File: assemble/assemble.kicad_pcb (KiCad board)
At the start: 2 copper layers, 283.6 x 105.3 mm, 94 parts, among them J1 Conn_01x04, SW1 SW_Push, SW10 SW_Push, SW11 SW_Push, SW12 SW_Push, SW13 SW_Push, SW14 SW_Push, SW15 SW_Push, SW16 SW_Push, SW17 SW_Push, SW18 SW_Push, SW19 SW_Push, SW2 SW_Push, SW20 SW_Push, SW21 SW_Push, SW22 SW_Push, SW23 SW_Push, SW24 SW_Push, SW25 SW_Push, SW26 SW_Push, SW27 SW_Push, SW28 SW_Push, SW29 SW_Push, SW3 SW_Push, SW30 SW_Push, SW31 SW_Push, SW32 SW_Push, SW33 SW_Push, SW34 SW_Push, SW35 SW_Push, SW36 SW_Push, SW37 SW_Push, SW38 SW_Push, SW39 SW_Push, SW4 SW_Push, SW40 SW_Push, SW41 SW_Push, SW42 SW_Push, SW45 RotaryEncoder_Switch, SW46 RotaryEncoder_Switch, SW47 SW_SPDT, SW5 SW_Push, SW6 SW_Push, SW7 SW_Push, SW8 SW_Push, SW9 SW_Push, U1 XIAO-nRF52840-SMD, U4 XIAO-nRF52840-SMD

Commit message: feat: implement schematic and PCB partially
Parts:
- removed U4: XIAO-nRF52840-SMD, xiao:XIAO-nRF52840-SMD
- added D43: D, kbd_Parts:Diode_SMD, F.Cu at (245.8, 104.6)
- added D44: D, kbd_Parts:Diode_SMD, F.Cu at (251.7, 104.6)
- added D45: D, kbd_Parts:Diode_SMD, F.Cu at (257.7, 104.6)
- added D46: D, kbd_Parts:Diode_SMD, F.Cu at (263.4, 112.6)
- added D47: D, kbd_Parts:Diode_SMD, F.Cu at (245.8, 112.6)
- added D48: D, kbd_Parts:Diode_SMD, F.Cu at (218.6, 52.2)
- added D49: D, kbd_Parts:Diode_SMD, F.Cu at (222.6, 69.4)
- added D50: D, kbd_Parts:Diode_SMD, F.Cu at (225.6, 85.8)
- added D51: D, kbd_Parts:Diode_SMD, F.Cu at (251.7, 112.6)
- added D52: D, kbd_Parts:Diode_SMD, F.Cu at (235.8, 52.6)
- added D53: D, kbd_Parts:Diode_SMD, F.Cu at (238.6, 69.4)
- added D54: D, kbd_Parts:Diode_SMD, F.Cu at (241.6, 86.0)
- added D55: D, kbd_Parts:Diode_SMD, F.Cu at (263.4, 104.6)
- added D56: D, kbd_Parts:Diode_SMD, F.Cu at (252.0, 52.6)
- added D57: D, kbd_Parts:Diode_SMD, F.Cu at (255.6, 69.2)
- added D58: D, kbd_Parts:Diode_SMD, F.Cu at (258.6, 85.8)
- added D59: D, kbd_Parts:Diode_SMD, F.Cu at (257.7, 112.6)
- added D60: D, kbd_Parts:Diode_SMD, F.Cu at (167.2, 119.2)
- added D61: D, kbd_Parts:Diode_SMD, F.Cu at (183.0, 112.7)
- added D62: D, kbd_Parts:Diode_SMD, F.Cu at (198.0, 106.4)
- added J2: Conn_01x05, Connector_PinHeader_1.00mm:PinHeader_1x05_P1.00mm_Vertical, F.Cu at (138.6, 41.8)
- added JP1: SolderJumper_2_Open, Jumper:SolderJumper-2_P1.3mm_Open_Pad1.0x1.5mm, F.Cu at (140.0, 126.8)
- added JP2: SolderJumper_2_Open, Jumper:SolderJumper-2_P1.3mm_Open_Pad1.0x1.5mm, F.Cu at (140.0, 132.8)
- added SW43: SW_Push, kicad-lib:Choc_v2_Hotswap_1u_16.6, F.Cu at (169.4, 124.4)
- added SW44: SW_Push, kicad-lib:Choc_v2_Hotswap_1u_16.6, F.Cu at (184.7, 118.0)
- added U2: XIAO-nRF52840-SMD, xiao:XIAO-nRF52840-SMD, F.Cu at (256.2, 128.1)
- BT1: footprint kbd_Parts:Battery_AAA -> Battery:BatteryHolder_Keystone_2460_1xAA
- R1, R2: footprint Resistor_THT:R_Axial_DIN0204_L3.6mm_D1.6mm_P5.08mm_Horizontal -> Resistor_SMD:R_0603_1608Metric_Pad0.98x0.95mm_HandSolder
- SW1, SW10, SW11, SW12, SW13, SW14, SW15, SW16, SW17, SW18, SW19, SW2, SW20, SW21, SW22, SW23, SW24, SW25, SW27, SW28, SW29, SW3, SW30, SW31, SW33, SW34, SW35, SW36, SW37, SW38, SW4, SW40, SW41, SW42, SW5, SW6, SW7, SW8, SW9: footprint kicad-lib:CherryMX-HotSwap-1u_17 -> kicad-lib:Choc_v2_Hotswap_1u_16.6
- SW26, SW39: value SW_Push -> RotaryEncoder_Switch; footprint kicad-lib:CherryMX-HotSwap-1u_17 -> kbd_Parts:RotaryEncoder_EC12E
- SW32: value SW_Push -> SW_SPDT; footprint kicad-lib:CherryMX-HotSwap-1u_17 -> kbd_Parts:TGSW_MSK-12D19
- SW45: value RotaryEncoder_Switch -> SW_Push; footprint kbd_Parts:RotaryEncoder_EC12E -> kicad-lib:Choc_v2_Hotswap_1u_16.6
- SW46: value RotaryEncoder_Switch -> SW_Push; footprint kbd_Parts:RotaryEncoder_EC12E -> kbd_Parts:ResetSW
- SW47: value SW_SPDT -> SW_Push; footprint kbd_Parts:TGSW_MSK-12D19 -> kbd_Parts:ResetSW
- moved SW46 201.7 mm to (41.8, 130.4), turned to 0 degrees
- moved SW26 159.2 mm to (54.5, 114.3), turned to 90 degrees
- moved SW45 145.1 mm to (200.0, 111.6), turned to 22.62 degrees
- moved D30 140.8 mm to (99.7, 113.2), turned to -22.62 degrees
- moved U1 136.2 mm to (24.5, 122.9), turned to 90 degrees
- moved D19 133.5 mm to (139.5, 109.4), turned to 90 degrees
- moved D42 128.8 mm to (157.2, 117.0), turned to -90 degrees
- moved SW47 122.2 mm to (237.0, 137.0)
- moved D32 120.8 mm to (114.4, 119.4), turned to -22.62 degrees
- moved D29 119.7 mm to (84.5, 106.9), turned to -22.62 degrees
- moved SW21 104.1 mm to (113.0, 124.4), turned to -22.62 degrees
- moved D28 103.1 mm to (108.7, 98.3), turned to -22.62 degrees
- moved D24 99.1 mm to (94.0, 92.4), turned to -22.62 degrees
- moved D13 95.8 mm to (133.4, 109.4), turned to 90 degrees
- moved SW20 95.5 mm to (97.7, 118.0), turned to -22.62 degrees
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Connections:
- AE-XCL102D333CR-G1 pad 3: Net-(SW47-B) -> Net-(SW32-B)
- D1 pad 1: ROW1L -> Net-(D1-K)
- D1 pad 2: Net-(D1-A) -> INTR_L
- D10 pad 1: ROW2L -> PIN1L
- D11 pad 1: ROW3L -> PIN1L
- D12 pad 1: ROW4L -> PIN1L
- D13 pad 2: ROW1L -> PIN2L
- D14 pad 1: Net-(D14-K) -> PIN2L
- D14 pad 2: ROW2L -> Net-(D14-A)
- D15 pad 1: Net-(D15-K) -> PIN2L
- D15 pad 2: ROW3L -> Net-(D15-A)
- D16 pad 1: Net-(D16-K) -> PIN2L
- D16 pad 2: ROW1L -> Net-(D16-A)
- D17 pad 1: Net-(D17-K) -> PIN2L
- D17 pad 2: ROW2L -> Net-(D17-A)
- D18 pad 1: Net-(D18-K) -> PIN2L
- D18 pad 2: ROW3L -> Net-(D18-A)
- D19 pad 2: ROW1L -> PIN3L
- D2 pad 1: ROW2L -> Net-(D13-K)
- D2 pad 2: Net-(D2-A) -> INTR_L
- D20 pad 1: Net-(D20-K) -> PIN3L
- D20 pad 2: ROW2L -> Net-(D20-A)
- D21 pad 1: Net-(D21-K) -> PIN3L
- D21 pad 2: ROW3L -> Net-(D21-A)
- D22 pad 1: Net-(D22-K) -> PIN3L
- D22 pad 2: ROW1R -> Net-(D22-A)
- D23 pad 1: Net-(D23-K) -> PIN3L
- D23 pad 2: ROW2R -> Net-(D23-A)
- D24 pad 1: Net-(D24-K) -> PIN3L
- D24 pad 2: ROW3R -> Net-(D24-A)
- D25 pad 2: ROW4R -> PIN4L
- D26 pad 1: Net-(D26-K) -> PIN4L
- D26 pad 2: ROW1R -> Net-(D26-A)
- D27 pad 1: Net-(D27-K) -> PIN4L
- D27 pad 2: ROW2R -> Net-(D27-A)
- D28 pad 1: Net-(D28-K) -> PIN4L
- D28 pad 2: ROW3R -> Net-(D28-A)
- D29 pad 1: Net-(D29-K) -> PIN4L
- D29 pad 2: ROW4R -> Net-(D29-A)
- D3 pad 1: ROW3L -> Net-(D19-K)
- D3 pad 2: Net-(D3-A) -> INTR_L
- D30 pad 1: Net-(D30-K) -> PIN4L
- D30 pad 2: ROW1R -> Net-(D30-A)
- D31 pad 2: ROW2R -> PIN5L
- D32 pad 1: Net-(D32-K) -> PIN5L
- D32 pad 2: ROW3R -> Net-(D32-A)
- D33 pad 1: Net-(D33-K) -> PIN5L
- D33 pad 2: ROW4R -> Net-(D33-A)
- D34 pad 1: ROW1R -> PIN5L
- D35 pad 1: ROW2R -> PIN5L
- D36 pad 1: ROW3R -> PIN5L
- D37 pad 1: ROW1R -> PIN6L
- D38 pad 1: ROW2R -> PIN6L
- D39 pad 1: ROW3R -> PIN6L
- D4 pad 1: ROW4L -> Net-(D25-K)
- D4 pad 2: Net-(D4-A) -> INTR_L
- D40 pad 1: ROW1R -> PIN6L
- D41 pad 1: ROW2R -> PIN6L
- D42 pad 1: ROW3R -> Net-(D42-K)
- D42 pad 2: Net-(D42-A) -> PIN6L
- D5 pad 1: ROW1L -> Net-(D31-K)
- D5 pad 2: Net-(D5-A) -> INTR_L
- D6 pad 1: ROW2L -> Net-(D42-K)
- D6 pad 2: Net-(D6-A) -> INTR_L
- D7 pad 1: ROW3L -> Net-(D1-K)
- D7 pad 2: Net-(D7-A) -> PIN1L
- D8 pad 1: ROW4L -> PIN1L
- D9 pad 1: ROW1L -> PIN1L
- R1 pad 2: SCL -> SDA
- R2 pad 2: SDA -> SCL
- SW1 pad 1: COL1L -> (no net)
- SW1 pad 2: Net-(D1-A) -> (no net)
- SW10 pad 1: COL3L -> (no net)
- SW10 pad 2: Net-(D10-A) -> (no net)
- SW11 pad 1: COL3L -> (no net)
- SW11 pad 2: Net-(D11-A) -> (no net)
- SW12 pad 1: COL3L -> (no net)
- SW12 pad 2: Net-(D12-A) -> (no net)
- SW13 pad 1: COL1L -> (no net)
- SW13 pad 2: Net-(D13-K) -> (no net)
- SW14 pad 1: COL1L -> (no net)
- SW14 pad 2: Net-(D14-K) -> (no net)
- SW15 pad 1: COL1L -> (no net)
- SW15 pad 2: Net-(D15-K) -> (no net)
- SW16 pad 1: COL2L -> (no net)
- SW16 pad 2: Net-(D16-K) -> (no net)
- SW17 pad 1: COL2L -> (no net)
- SW17 pad 2: Net-(D17-K) -> (no net)
- SW18 pad 1: COL2L -> (no net)
- SW18 pad 2: Net-(D18-K) -> (no net)
- SW19 pad 1: COL3L -> (no net)
- SW19 pad 2: Net-(D19-K) -> (no net)
- SW2 pad 1: COL1L -> (no net)
- SW2 pad 2: Net-(D2-A) -> (no net)
- SW20 pad 1: COL3L -> (no net)
- SW20 pad 2: Net-(D20-K) -> (no net)
- SW21 pad 1: COL3L -> (no net)
- SW21 pad 2: Net-(D21-K) -> (no net)
- SW22 pad 1: COL1R -> (no net)
- SW22 pad 2: Net-(D22-K) -> (no net)
- SW23 pad 1: COL1R -> (no net)
- SW23 pad 2: Net-(D23-K) -> (no net)
- SW24 pad 1: COL1R -> (no net)
- SW24 pad 2: Net-(D24-K) -> (no net)
- SW25 pad 1: COL1R -> (no net)
- SW25 pad 2: Net-(D25-K) -> (no net)
- SW27 pad 1: COL2R -> (no net)
- SW27 pad 2: Net-(D27-K) -> (no net)
- SW28 pad 1: COL2R -> (no net)
- SW28 pad 2: Net-(D28-K) -> (no net)
- SW29 pad 1: COL2R -> (no net)
- SW29 pad 2: Net-(D29-K) -> (no net)
- SW3 pad 1: COL1L -> (no net)
- SW3 pad 2: Net-(D3-A) -> (no net)
- SW30 pad 1: COL3R -> (no net)
- SW30 pad 2: Net-(D30-K) -> (no net)
- SW31 pad 1: COL3R -> (no net)
- SW31 pad 2: Net-(D31-K) -> (no net)
- SW32 pad 1: COL3R -> unconnected-(SW32-A-Pad1)
- SW32 pad 2: Net-(D32-K) -> Net-(SW32-B)
- SW33 pad 1: COL3R -> (no net)
- SW33 pad 2: Net-(D33-K) -> (no net)
- SW34 pad 1: COL1R -> (no net)
- SW34 pad 2: Net-(D34-A) -> (no net)
- SW35 pad 1: COL1R -> (no net)
- SW35 pad 2: Net-(D35-A) -> (no net)
- SW36 pad 1: COL1R -> (no net)
- SW36 pad 2: Net-(D36-A) -> (no net)
- SW37 pad 1: COL2R -> (no net)
- SW37 pad 2: Net-(D37-A) -> (no net)
- SW38 pad 1: COL2R -> (no net)
- SW38 pad 2: Net-(D38-A) -> (no net)
- SW4 pad 1: COL1L -> (no net)
- SW4 pad 2: Net-(D4-A) -> (no net)
- SW40 pad 1: COL3R -> (no net)
- SW40 pad 2: Net-(D40-A) -> (no net)
- SW41 pad 1: COL3R -> (no net)
- SW41 pad 2: Net-(D41-A) -> (no net)
- SW42 pad 1: COL3R -> (no net)
- SW42 pad 2: Net-(D42-A) -> (no net)
- SW47 pad 1: unconnected-(SW47-A-Pad1) -> RST_GND_R
- SW47 pad 2: Net-(SW47-B) -> RST_R
- SW5 pad 1: COL2L -> (no net)
- SW5 pad 2: Net-(D5-A) -> (no net)
- SW6 pad 1: COL2L -> (no net)
- SW6 pad 2: Net-(D6-A) -> (no net)
- SW7 pad 1: COL2L -> (no net)
- SW7 pad 2: Net-(D7-A) -> (no net)
- SW8 pad 1: COL2L -> (no net)
- SW8 pad 2: Net-(D8-A) -> (no net)
- SW9 pad 1: COL3L -> (no net)
- SW9 pad 2: Net-(D9-A) -> (no net)
- U1 pad 10: ROW2L -> PIN3L
- U1 pad 11: ROW1L -> PIN2L
- U1 pad 17: unconnected-(U1-NFC1-Pad17) -> PIN5L
- U1 pad 18: unconnected-(U1-NFC2-Pad18) -> PIN6L
- U1 pad 21: unconnected-(U1-RESET-Pad21) -> RST_L
- U1 pad 22: unconnected-(U1-GND-Pad22) -> RST_GND_L
- U1 pad 3: COL1L -> INTR_L
- U1 pad 4: COL2L -> PIN1L
- U1 pad 7: COL3L -> TX_L
- U1 pad 8: ROW4L -> RX_L
- U1 pad 9: ROW3L -> PIN4L
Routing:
- net COL3R: track 268.7 -> 0.00 mm, vias 18 -> 0
- net COL3L: track 255.7 -> 0.00 mm, vias 6 -> 0
- net GNDR: track 238.8 -> 0.00 mm, vias 6 -> 0
- net COL1L: track 236.8 -> 0.00 mm, vias 5 -> 0
- net COL2R: track 232.5 -> 0.00 mm, vias 16 -> 0
- net COL1R: track 227.1 -> 0.00 mm, vias 18 -> 0
- net ROW2R: track 216.6 -> 0.00 mm, vias 14 -> 0
- net GNDL: track 212.2 -> 0.00 mm, vias 5 -> 0
- net RE2B: track 198.6 -> 0.00 mm, vias 2 -> 0
- net ROW3L: track 198.3 -> 0.00 mm, vias 21 -> 0
- net ROW3R: track 197.7 -> 0.00 mm, vias 10 -> 0
- net RE2A: track 193.0 -> 0.00 mm, vias 2 -> 0
- net RE1B: track 190.1 -> 0.00 mm, vias 5 -> 0
- net COL2L: track 188.8 -> 0.00 mm, vias 3 -> 0
- net RE1A: track 188.5 -> 0.00 mm, vias 3 -> 0
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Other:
- board size 283.6 x 105.3 mm -> 40 x 40 mm
- board text removed: "ON"
- board text removed: "Orbit One v2.0 Designed by derui"

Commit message: feat: implement some features
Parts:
- BT1, JP1, JP2, U1, U2: moved to B.Cu
- J2: footprint Connector_PinHeader_1.00mm:PinHeader_1x05_P1.00mm_Vertical -> Connector_PinHeader_2.00mm:PinHeader_1x05_P2.00mm_Vertical
- moved D46 98.7 mm to (164.8, 109.2)
- moved D55 98.6 mm to (164.8, 101.6)
- moved D59 97.7 mm to (160.1, 109.2)
- moved D45 97.6 mm to (160.1, 101.6)
- moved D51 96.4 mm to (155.3, 109.2)
- moved D44 96.4 mm to (155.3, 101.6)
- moved D47 95.3 mm to (150.6, 109.2)
- moved D43 95.3 mm to (150.6, 101.6)
- moved BT1 71.1 mm to (186.0, 48.4), turned to 180 degrees
- moved AE-XCL102D333CR-G1 35.4 mm to (147.2, 61.8)
- moved SW46 18.9 mm to (60.5, 127.3), turned to 180 degrees
- moved J2 14.8 mm to (128.2, 52.4), turned to 180 degrees
- moved D10 12.4 mm to (29.0, 96.8)
- moved D8 12.4 mm to (35.7, 63.6)
- moved D9 12.4 mm to (32.3, 80.2)
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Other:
- board size 40 x 40 mm -> 264.4 x 104.6 mm

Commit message: feat: implement PCB
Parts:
- R1, R2: moved to B.Cu
- moved D55 17.1 mm to (157.3, 117.0)
- moved D45 17.1 mm to (152.6, 117.0)
- moved D59 7.84 mm to (162.0, 101.6), turned to 90 degrees
- moved D46 2.81 mm to (162.0, 109.4)
- moved D4 2.00 mm to (147.0, 109.1)
- moved D5 2.00 mm to (142.6, 109.1)
- moved D1 2.00 mm to (137.8, 116.6)
- moved D13 2.00 mm to (133.4, 101.6)
- moved D19 2.00 mm to (137.8, 101.6)
- moved D2 2.00 mm to (133.4, 109.1)
- moved D25 2.00 mm to (147.0, 101.6)
- moved D3 2.00 mm to (137.8, 109.1)
- moved D31 2.00 mm to (142.6, 101.6)
- moved D42 2.00 mm to (147.0, 116.8)
- moved D43 2.00 mm to (152.6, 101.6), turned to 90 degrees
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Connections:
- J1 pad 2: VCC -> VCCL
- J2 pad 3: VCC -> VCCR
- R1 pad 1: VCC -> VCCL
- R2 pad 1: VCC -> VCCL
- SW1 pad 1: (no net) -> Net-(D13-K)
- SW1 pad 2: (no net) -> Net-(D8-A)
- SW10 pad 1: (no net) -> Net-(D42-K)
- SW10 pad 2: (no net) -> Net-(D18-A)
- SW11 pad 1: (no net) -> Net-(D1-K)
- SW11 pad 2: (no net) -> Net-(D20-A)
- SW12 pad 1: (no net) -> Net-(D13-K)
- SW12 pad 2: (no net) -> Net-(D21-A)
- SW13 pad 1: (no net) -> Net-(D25-K)
- SW13 pad 2: (no net) -> Net-(D22-A)
- SW14 pad 1: (no net) -> Net-(D31-K)
- SW14 pad 2: (no net) -> Net-(D23-A)
- SW15 pad 1: (no net) -> Net-(D42-K)
- SW15 pad 2: (no net) -> Net-(D24-A)
- SW16 pad 1: (no net) -> Net-(D31-K)
- SW16 pad 2: (no net) -> Net-(D26-A)
- SW17 pad 1: (no net) -> Net-(D42-K)
- SW17 pad 2: (no net) -> Net-(D27-A)
- SW18 pad 1: (no net) -> Net-(D1-K)
- SW18 pad 2: (no net) -> Net-(D28-A)
- SW19 pad 1: (no net) -> Net-(D13-K)
- SW19 pad 2: (no net) -> Net-(D29-A)
- SW2 pad 1: (no net) -> Net-(D19-K)
- SW2 pad 2: (no net) -> Net-(D9-A)
- SW20 pad 1: (no net) -> Net-(D19-K)
- SW20 pad 2: (no net) -> Net-(D30-A)
- SW21 pad 1: (no net) -> Net-(D1-K)
- SW21 pad 2: (no net) -> Net-(D32-A)
- SW22 pad 1: (no net) -> Net-(D13-K)
- SW22 pad 2: (no net) -> Net-(D33-A)
- SW23 pad 1: (no net) -> Net-(D19-K)
- SW23 pad 2: (no net) -> Net-(D34-A)
- SW24 pad 1: (no net) -> Net-(D25-K)
- SW24 pad 2: (no net) -> Net-(D35-A)
- SW25 pad 1: (no net) -> Net-(D42-K)
- SW25 pad 2: (no net) -> Net-(D36-A)
- SW27 pad 1: (no net) -> Net-(D1-K)
- SW27 pad 2: (no net) -> Net-(D37-A)
- SW28 pad 1: (no net) -> Net-(D13-K)
- SW28 pad 2: (no net) -> Net-(D38-A)
- SW29 pad 1: (no net) -> Net-(D19-K)
- SW29 pad 2: (no net) -> Net-(D39-A)
- SW3 pad 1: (no net) -> Net-(D25-K)
- SW3 pad 2: (no net) -> Net-(D10-A)
- SW30 pad 1: (no net) -> Net-(D25-K)
- SW30 pad 2: (no net) -> Net-(D40-A)
- SW31 pad 1: (no net) -> Net-(D31-K)
- SW31 pad 2: (no net) -> Net-(D41-A)
- SW33 pad 1: (no net) -> Net-(D44-K)
- SW33 pad 2: (no net) -> Net-(D48-A)
- SW34 pad 1: (no net) -> Net-(D45-K)
- SW34 pad 2: (no net) -> Net-(D49-A)
- SW35 pad 1: (no net) -> Net-(D46-K)
- SW35 pad 2: (no net) -> Net-(D50-A)
- SW36 pad 1: (no net) -> Net-(D43-K)
- SW36 pad 2: (no net) -> Net-(D52-A)
- SW37 pad 1: (no net) -> Net-(D45-K)
- SW37 pad 2: (no net) -> Net-(D53-A)
- SW38 pad 1: (no net) -> Net-(D46-K)
- SW38 pad 2: (no net) -> Net-(D54-A)
- SW4 pad 1: (no net) -> Net-(D31-K)
- SW4 pad 2: (no net) -> Net-(D11-A)
- SW40 pad 1: (no net) -> Net-(D43-K)
- SW40 pad 2: (no net) -> Net-(D56-A)
- SW41 pad 1: (no net) -> Net-(D44-K)
- SW41 pad 2: (no net) -> Net-(D57-A)
- SW42 pad 1: (no net) -> Net-(D46-K)
- SW42 pad 2: (no net) -> Net-(D58-A)
- SW43 pad 1: (no net) -> Net-(D43-K)
- SW43 pad 2: (no net) -> Net-(D60-A)
- SW44 pad 1: (no net) -> Net-(D44-K)
- SW44 pad 2: (no net) -> Net-(D61-A)
- SW45 pad 1: (no net) -> Net-(D45-K)
- SW45 pad 2: (no net) -> Net-(D62-A)
- SW5 pad 1: (no net) -> Net-(D42-K)
- SW5 pad 2: (no net) -> Net-(D12-A)
- SW6 pad 1: (no net) -> Net-(D1-K)
- SW6 pad 2: (no net) -> Net-(D14-A)
- SW7 pad 1: (no net) -> Net-(D19-K)
- SW7 pad 2: (no net) -> Net-(D15-A)
- SW8 pad 1: (no net) -> Net-(D25-K)
- SW8 pad 2: (no net) -> Net-(D16-A)
- SW9 pad 1: (no net) -> Net-(D31-K)
- SW9 pad 2: (no net) -> Net-(D17-A)
- U1 pad 12: VCC -> VCCL
- U2 pad 12: VCC -> VCCR
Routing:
- net BAT-: track 0.00 -> 371.8 mm, vias 0 -> 9
- net Net-(D19-K): track 0.00 -> 363.6 mm, vias 0 -> 17
- net BAT+: track 0.00 -> 348.9 mm, vias 0 -> 8
- net PIN3R: track 0.00 -> 319.6 mm, vias 0 -> 20
- net Net-(D13-K): track 0.00 -> 307.6 mm, vias 0 -> 18
- net PIN6L: track 0.00 -> 305.2 mm, vias 0 -> 19
- net Net-(D31-K): track 0.00 -> 295.1 mm, vias 0 -> 18
- net Net-(D1-K): track 0.00 -> 293.0 mm, vias 0 -> 17
- net INTR_L: track 0.00 -> 286.8 mm, vias 0 -> 16
- net Net-(D25-K): track 0.00 -> 284.1 mm, vias 0 -> 18
- net PIN5L: track 0.00 -> 283.4 mm, vias 0 -> 25
- net Net-(D42-K): track 0.00 -> 277.6 mm, vias 0 -> 16
- net GNDR: track 0.00 -> 274.8 mm, vias 0 -> 9
- net PIN1R: track 0.00 -> 273.8 mm, vias 0 -> 20
- net PIN1L: track 0.00 -> 272.0 mm, vias 0 -> 15
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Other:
- outline, holes or cut-outs redrawn

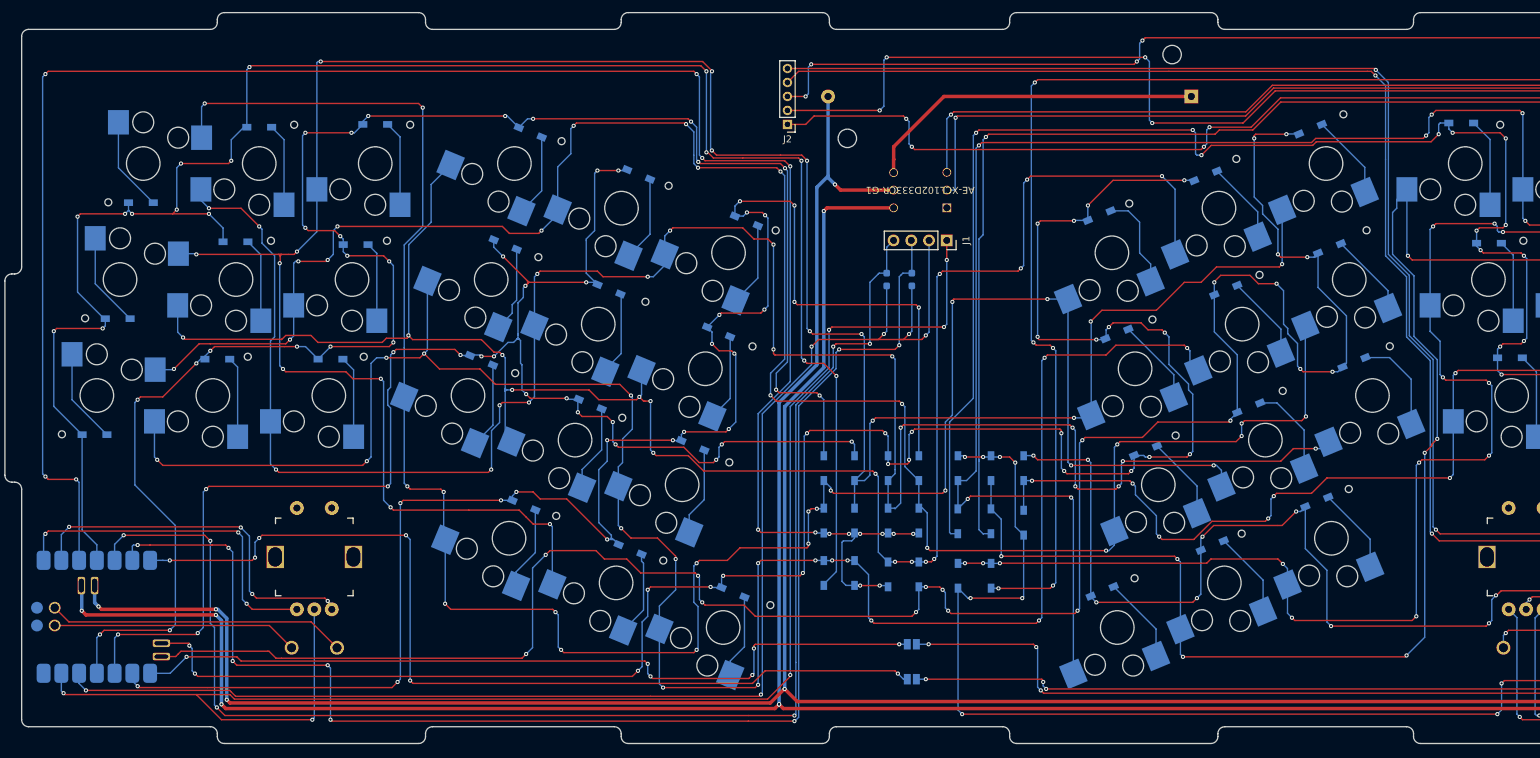
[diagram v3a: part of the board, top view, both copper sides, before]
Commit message: fix: update screw in PCB
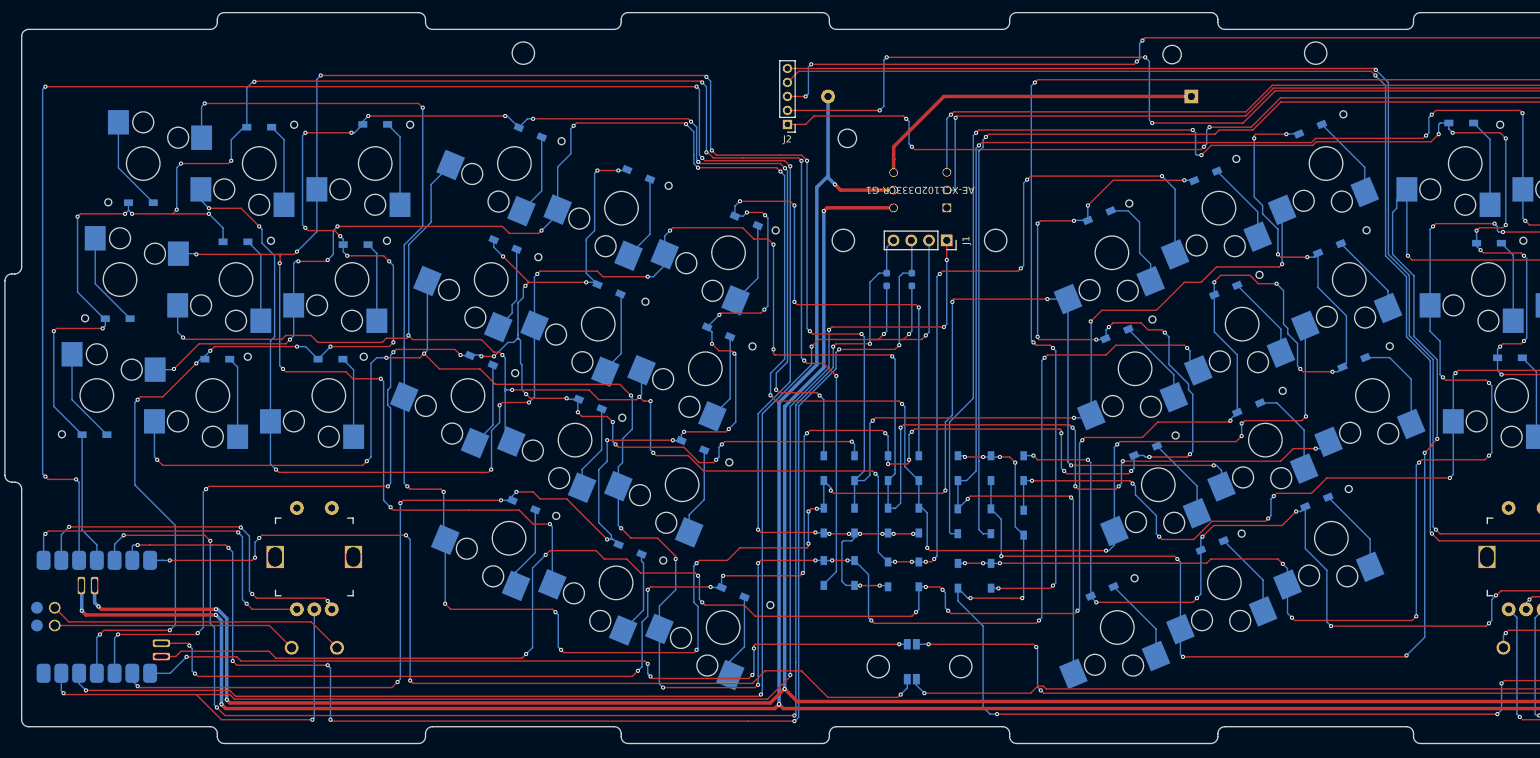
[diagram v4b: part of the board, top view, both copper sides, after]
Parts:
- added Ref**: Val**, kbd_Hole:m3_Screw_Hole_EdgeCuts, F.Cu at (90.4, 42.2)
- added Ref**: Val**, kbd_Hole:m3_Screw_Hole_EdgeCuts, F.Cu at (203.8, 42.2)
- added Ref**: Val**, kbd_Hole:m3_Screw_Hole_EdgeCuts, F.Cu at (153.0, 130.0)
- added Ref**: Val**, kbd_Hole:m3_Screw_Hole_EdgeCuts, F.Cu at (136.2, 69.0)
- added Ref**: Val**, kbd_Hole:m3_Screw_Hole_EdgeCuts, F.Cu at (158.0, 69.0)
- added Ref**: Val**, kbd_Hole:m3_Screw_Hole_EdgeCuts, F.Cu at (141.2, 130.0)
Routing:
- net PIN1L: track 272.0 -> 267.4 mm
- net Net-(D19-K): track 363.6 -> 359.4 mm
- net INTR_L: track 286.8 -> 282.8 mm
- net TX_L: track 133.0 -> 135.9 mm
- net INTR_R: track 180.3 -> 178.0 mm
- net RX_R: track 129.7 -> 130.6 mm, vias 6 -> 4

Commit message: feat: add switch plate
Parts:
- moved Ref** 2.00 mm to (92.4, 42.2)
- moved U1 1.99 mm to (31.4, 122.9)
- moved Ref** 1.00 mm to (154.0, 130.0)
- moved Ref** 1.00 mm to (137.2, 69.0)
- moved JP1 0.35 mm to (146.3, 126.8)
- moved JP2 0.35 mm to (146.3, 131.8)
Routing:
- net BAT-: track 371.8 -> 369.1 mm
- net GNDL: track 223.8 -> 221.3 mm
- net RE1B: track 52.7 -> 50.4 mm
- net PIN4L: track 244.7 -> 242.4 mm
- net PIN3L: track 219.9 -> 217.6 mm
- net SCL: track 202.0 -> 199.8 mm
- net PIN6L: track 305.2 -> 303.0 mm
- net SDA: track 201.7 -> 199.6 mm
- net PIN2L: track 259.2 -> 257.1 mm
- net RE1A: track 50.0 -> 47.8 mm
- net RST_L: track 42.8 -> 40.8 mm
- net RST_GND_L: track 35.2 -> 33.2 mm
- net TX_L: track 135.9 -> 137.8 mm
- net BAT+: track 348.9 -> 347.0 mm
- net VCCL: track 201.7 -> 199.8 mm
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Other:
- board size 264.4 x 104.6 mm -> 262.4 x 104.6 mm

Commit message: refactor: start re-wiring
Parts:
- moved BT1 11.9 mm to (174.1, 48.4)
- moved J2 3.20 mm to (131.4, 52.4)
- moved AE-XCL102D333CR-G1 1.80 mm to (149.0, 61.8)
- moved D22 1.80 mm to (108.7, 59.6)
- moved D25 1.80 mm to (148.8, 101.6)
- moved D31 1.80 mm to (144.4, 101.6)
- moved D4 1.80 mm to (148.8, 109.1)
- moved D42 1.80 mm to (148.8, 116.8)
- moved D43 1.80 mm to (154.4, 101.6)
- moved D46 1.80 mm to (163.8, 109.4)
- moved D47 1.80 mm to (154.4, 109.2)
- moved D5 1.80 mm to (144.4, 109.1)
- moved D51 1.80 mm to (159.1, 109.2)
- moved D55 1.80 mm to (159.1, 117.0)
- moved D59 1.80 mm to (163.8, 101.6)
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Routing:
- net BAT-: track 369.1 -> 0.00 mm, vias 9 -> 0
- net Net-(D19-K): track 359.4 -> 0.00 mm, vias 17 -> 0
- net BAT+: track 347.0 -> 0.00 mm, vias 8 -> 0
- net PIN3R: track 319.6 -> 0.00 mm, vias 20 -> 0
- net Net-(D13-K): track 307.6 -> 0.00 mm, vias 18 -> 0
- net PIN6L: track 303.0 -> 0.00 mm, vias 19 -> 0
- net Net-(D31-K): track 295.1 -> 0.00 mm, vias 18 -> 0
- net Net-(D1-K): track 293.0 -> 0.00 mm, vias 17 -> 0
- net Net-(D25-K): track 284.1 -> 0.00 mm, vias 18 -> 0
- net PIN5L: track 281.7 -> 0.00 mm, vias 25 -> 0
- net INTR_L: track 281.4 -> 0.00 mm, vias 16 -> 0
- net Net-(D42-K): track 277.6 -> 0.00 mm, vias 16 -> 0
- net GNDR: track 274.8 -> 0.00 mm, vias 9 -> 0
- net PIN1R: track 273.8 -> 0.00 mm, vias 20 -> 0
- net PIN1L: track 268.2 -> 0.00 mm, vias 15 -> 0
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
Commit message: refactor: finish re-wiring
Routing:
- net BAT-: track 0.00 -> 385.8 mm, vias 0 -> 8
- net Net-(D31-K): track 0.00 -> 360.8 mm, vias 0 -> 16
- net PIN3L: track 0.00 -> 357.0 mm, vias 0 -> 12
- net BAT+: track 0.00 -> 340.7 mm, vias 0 -> 6
- net Net-(D42-K): track 0.00 -> 303.3 mm, vias 0 -> 18
- net PIN1L: track 0.00 -> 298.5 mm, vias 0 -> 18
- net Net-(D25-K): track 0.00 -> 288.0 mm, vias 0 -> 14
- net Net-(D19-K): track 0.00 -> 285.9 mm, vias 0 -> 14
- net Net-(D13-K): track 0.00 -> 280.5 mm, vias 0 -> 12
- net PIN2L: track 0.00 -> 272.8 mm, vias 0 -> 14
- net PIN6L: track 0.00 -> 269.2 mm, vias 0 -> 11
- net GNDR: track 0.00 -> 261.8 mm, vias 0 -> 7
- net Net-(D1-K): track 0.00 -> 260.0 mm, vias 0 -> 18
- net PIN1R: track 0.00 -> 256.3 mm, vias 0 -> 12
- net PIN5L: track 0.00 -> 253.5 mm, vias 0 -> 14
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
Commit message: fix: update switch plate
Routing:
- net Net-(D31-K): track 360.8 -> 359.4 mm
- net TX_R: track 116.9 -> 117.9 mm
- net RX_L: track 113.0 -> 113.9 mm
- net RX_R: track 128.5 -> 129.2 mm
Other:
- board text added: "ON"
